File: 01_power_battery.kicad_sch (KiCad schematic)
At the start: 144 parts, among them Q13 CSD19537Q3 100V AUX reverse F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, Q14 BSS138 fast reverse-gate pull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, Q21 SiSS4409DN 40V reverse-blocki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, Q22 SiSS4409DN 40V reverse-blocki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, Q23 SiSS4409DN 40V reverse-blocki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, Q24 SiSS4409DN 40V reverse-blocki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, Q25 CSD17575Q3 BQ25798 ship FET, Q26 SiSS4409DN 40V reverse-blocki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, Q27 SiSS4409DN 40V reverse-blocki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, Q28 SiSS4409DN 40V reverse-blocki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, Q29 SiSS4409DN 40V reverse-blocki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, Q700 BSS138 source and cell-temper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, Q702 BSS138 QON open-drain pulse, U10 BQ34Z100-G1 protected-pack ga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, U12 TPS26630RGER 3A AUX eFuse / s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, U15 LTC4418IUF#PBF dual-input sel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, U16 LTC4418IUF#PBF dual-input sel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, U2 BQ25798RQMR, U2210 SN74LVC1G08DBVR charger reque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, U718 TPS26600RHFR aggregate AON eF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

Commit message: rework the board placement and fix more power stuff
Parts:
- removed D710, D712, D713: B340A 3A 40V EC always-on OR, Diode_SMD:D_SMA, symbol Device:D_Schottky
- removed D715: BAT54WS case button to charger QON, Diode_SMD:D_SOD-323, symbol Device:D_Schottky
- removed R17: 47.0k 0.02% 5ppm ILIM top (3.0A nominal setting), Resistor_SMD:R_0603_1608Metric, symbol Device:R
- removed R190: 100k 0.02% 5ppm ILIM bottom, Resistor_SMD:R_0603_1608Metric, symbol Device:R
- removed R705: 7.50k 1% fixed-valid TS bottom, Resistor_SMD:R_0603_1608Metric, symbol Device:R
- added C2600: 4.7u 50V X7R DCIN, Capacitor_SMD:C_1206_3216Metric, symbol Device:C
- added C2601: 4.7u 10V X7R VDDP, Capacitor_SMD:C_0805_2012Metric, symbol Device:C
- added C2602: 1n 50V C0G PROG filter, Capacitor_SMD:C_0402_1005Metric, symbol Device:C
- added C2603: 100n 50V input sense filter, Capacitor_SMD:C_0402_1005Metric, symbol Device:C
- added C2604: 100n 50V battery sense filter, Capacitor_SMD:C_0402_1005Metric, symbol Device:C
- added C2605: 22n 50V C0G forward compensation, Capacitor_SMD:C_0805_2012Metric, symbol Device:C
- added C2606: 47n 50V X7R reverse compensation, Capacitor_SMD:C_0603_1608Metric, symbol Device:C
- added C2607: 220n 50V X7R current monitor, Capacitor_SMD:C_0603_1608Metric, symbol Device:C
- added C2608, C2609: 100u 35V hybrid system bulk, Capacitor_SMD:CP_Elec_6.3x7.7, symbol Device:C_Polarized
- added C2620, C2621, C2650: 100n 50V charge pump, Capacitor_SMD:C_0603_1608Metric, symbol Device:C
- added C2622: 22n 50V C0G retry timer, Capacitor_SMD:C_0805_2012Metric, symbol Device:C
- added C2641, C2642, C2643: 100n 50V bypass, Capacitor_SMD:C_0603_1608Metric, symbol Device:C
- added C2651: 1u 50V protected input bypass, Capacitor_SMD:C_0603_1608Metric, symbol Device:C
- added C2660: 22n 50V C0G gate ramp, Capacitor_SMD:C_0805_2012Metric, symbol Device:C
- added C2661, C2662: 1u 50V fault timer, Capacitor_SMD:C_0603_1608Metric, symbol Device:C
- added C2685: 100n 50V U15 V2 local, Capacitor_SMD:C_0603_1608Metric, symbol Device:C
- added D2600, D2601: BAT54WS bias OR, Diode_SMD:D_SOD-323, symbol Device:D_Schottky
- added D2620: BAT54WS fast gate discharge, Diode_SMD:D_SOD-323, symbol Device:D_Schottky
- added D2640: BAT54S AUX ADC rail clamps, Package_TO_SOT_SMD:SOT-23, symbol BMS_Thermal:BAT54S_AKC
- added Q2600, Q2601, Q2602, Q2603: CSD17577Q3A 30V switching FET, ducktop2:CSD17577Q3A_DNH, symbol Q_NMOS_123S_4G_5678D:Q_NMOS_123S_4G_5678D
- added Q2604, Q2605: BSS138, Package_TO_SOT_SMD:SOT-23, symbol Q_NMOS_SOT23_GSD:Q_NMOS_SOT23_GSD
- added Q2620, Q2621, Q2622, Q2623, Q2650: CSD19537Q3 100V, ducktop2:CSD19537Q3_DQG, symbol Q_NMOS_123S_4G_5678D:Q_NMOS_123S_4G_5678D
- added Q2644: BSS138 AUX discharge, Package_TO_SOT_SMD:SOT-23, symbol Q_NMOS_SOT23_GSD:Q_NMOS_SOT23_GSD
- added Q2660: CSD18540Q5B AON pass FET, ducktop2:CSD18540Q5B_DNK, symbol Q_NMOS_123S_4G_5678D:Q_NMOS_123S_4G_5678D
- added R2600: 100k BGATE to source, Resistor_SMD:R_0603_1608Metric, symbol Device:R
- added R2601: 10R DCIN filter, Resistor_SMD:R_0603_1608Metric, symbol Device:R
- added R2602: 4.7R VDDP filter, Resistor_SMD:R_0603_1608Metric, symbol Device:R
- added R2603, R2604, R2605, R2606: 0R gate link, Resistor_SMD:R_0603_1608Metric, symbol Device:R
- added R2607: 2R input sense filter, Resistor_SMD:R_0402_1005Metric, symbol Device:R
- added R2608: 1k forward compensation, Resistor_SMD:R_0402_1005Metric, symbol Device:R
- added R2609: 1k reverse compensation, Resistor_SMD:R_0402_1005Metric, symbol Device:R
- added R2610: 4.53k current monitor filter, Resistor_SMD:R_0402_1005Metric, symbol Device:R
- added R2611: 20k PSYS monitor load, Resistor_SMD:R_0402_1005Metric, symbol Device:R
- added R2612: 100k throttle default-on, Resistor_SMD:R_0603_1608Metric, symbol Device:R
- added R2620: 10k gate ramp resistor, Resistor_SMD:R_0603_1608Metric, symbol Device:R
- added R2640: 100k 1% bias sense top, Resistor_SMD:R_0603_1608Metric, symbol Device:R
- added R2641: 24.9k 1% bias sense bottom, Resistor_SMD:R_0603_1608Metric, symbol Device:R
- added R2642: 10k bias-good pull-up, Resistor_SMD:R_0603_1608Metric, symbol Device:R
- added R2643: 100k PROCHOT sense default-low, Resistor_SMD:R_0603_1608Metric, symbol Device:R
- added R2644: 10k AUX permission series, Resistor_SMD:R_0603_1608Metric, symbol Device:R
- added R2645: 47k AUX permission default-off, Resistor_SMD:R_0603_1608Metric, symbol Device:R
- added R2646: 1k 1W switched AUX discharge, Resistor_SMD:R_2512_6332Metric, symbol Device:R
- added R2647: 100k discharge gate default-low, Resistor_SMD:R_0603_1608Metric, symbol Device:R
- added R2661: 10R gate damping, Resistor_SMD:R_0402_1005Metric, symbol Device:R
- added R2662, RS2660: 180m 1% 0.25W parallel AON shunt, Resistor_SMD:R_1206_3216Metric, symbol Device:R
- added R2663: 100k always-on enable, Resistor_SMD:R_0603_1608Metric, symbol Device:R
- added R2664: 1k gate-ramp branch, Resistor_SMD:R_0603_1608Metric, symbol Device:R
- added RS2600: 20m 1% 2W input Kelvin shunt, Resistor_SMD:R_2512_6332Metric, symbol Device:R
- added RS2601: 10m 1% 2W battery Kelvin shunt, Resistor_SMD:R_2512_6332Metric, symbol Device:R
- added RS2620: 22m 1% 2W AON Kelvin shunt, Resistor_SMD:R_2512_6332Metric, symbol Device:R
- added TP2660: AON reset, TestPoint:TestPoint_Pad_D1.5mm, symbol Connector:TestPoint
- added TP2661: GND, TestPoint:TestPoint_Pad_D1.5mm, symbol Connector:TestPoint
- added U2620, U2621: LM74700QDBVRQ1, Package_TO_SOT_SMD:SOT-23-6, symbol Power_Management:LM74700
- added U2634: TPS3700DDCR charger-bias detector, Package_TO_SOT_SMD:SOT-23-6, symbol TPS3700:TPS3700
- added U2635: TCA9537DGSR power status and AUX control, Package_SO:MSOP-10_3x3mm_P0.5mm, symbol Interface_Expansion:PCA9537
- added U2644: SN74LVC1G04DBVR AUX discharge, Package_TO_SOT_SMD:SOT-23-5, symbol 74xGxx:74LVC1G04
- added U2650: LM74700QDBVRQ1 system standby feed, Package_TO_SOT_SMD:SOT-23-6, symbol Power_Management:LM74700
- added U2660: LTC4231IMS-1#PBF standby current limiter, Package_SO:MSOP-12_3x4.039mm_P0.65mm, symbol LTC4231-1:LTC4231-1
- C10: value 100n 50V X7R PMID local -> 1u 50V input local; MPN GRM188R71H104KA93D -> GRT188R61H105ME13D
- C11: value 100n 50V X7R SYS local -> 1u 50V system local; MPN GRM188R71H104KA93D -> GRT188R61H105ME13D
- C2260: value 100n 50V charger-temperature AND bypass -> 100n 50V AND bypass
- C7: value 47n 25V X7R BTST1 -> 470n 25V X7R bootstrap; footprint Capacitor_SMD:C_0402_1005Metric -> Capacitor_SMD:C_0603_1608Metric; MPN GRM155R71E473KA88D -> C1608X7R1E474K080AE; Manufacturer Murata -> TDK
- C701, C702: value 10u 25V X7R VBUS -> 10u 50V X7R input; MPN GRM31CR71E106KA12L -> CGA5L1X7R1H106K160AC; Manufacturer Murata -> TDK
- C703, C704, C705: value 10u 25V X7R PMID -> 10u 50V X7R input; MPN GRM31CR71E106KA12L -> CGA5L1X7R1H106K160AC; Manufacturer Murata -> TDK
- C706, C707, C708, C709, C710: value 10u 25V X7R SYS -> 10u 25V X7R system
- C711: value 100n 50V X7R BAT local -> 100n 50V battery voltage filter; footprint Capacitor_SMD:C_0603_1608Metric -> Capacitor_SMD:C_0402_1005Metric; MPN GRM188R71H104KA93D -> GRM155R71H104ME14D
- C712, C713: value 10u 25V X7R BAT -> 10u 25V X7R battery
- C714: value 2.2u 25V X7R VBUS hot-plug damper -> 2.2u 50V X7R input damper; MPN GRM21BR71E225KA73L -> MSASU21GBB7225KTNA01; Manufacturer Murata -> Taiyo Yuden
- C715: value 15n 50V stage2 TMR approx 240ms -> 1n 50V C0G stage2 validation; MPN GRM155R71H153KA12D -> GRM1555C1H102JA01D
- C740: value 100n 10V INTVCC -> 100n 50V INTVCC; MPN GRM188R71A104KA61D -> GRM188R71H104KA93D
- C741: value 15n 50V TMR approx 240ms -> 1n 50V C0G selector validation; MPN GRM155R71H153KA12D -> GRM1555C1H102JA01D
- C749: value 100n 10V stage2 INTVCC -> 100n 50V stage2 INTVCC; MPN GRM188R71A104KA61D -> GRM188R71H104KA93D
- C795: value 1u 25V AON eFuse input -> 1u 50V AON input; footprint Capacitor_SMD:C_0805_2012Metric -> Capacitor_SMD:C_0603_1608Metric; MPN GRM21BR71H105KA12L -> GRT188R61H105ME13D
- C796: value 100n 50V AON eFuse input local -> 100n 50V AON input local
- C797: value 10u 25V AON eFuse output -> 100u 35V hybrid AON hold-up; footprint Capacitor_SMD:C_1206_3216Metric -> Capacitor_SMD:CP_Elec_6.3x7.7; symbol Device:C -> Device:C_Polarized; MPN GRM31CR71E106KA12L -> EEHZK1V101XP; Manufacturer Murata -> Panasonic
- C798: value 100n 50V AON eFuse output local -> 100n 50V AON output local
- C799: value 22n 50V C0G 5% AON eFuse dVdt -> 22n 50V C0G gate ramp
- C8: value 47n 25V X7R BTST2 -> 470n 25V X7R bootstrap; footprint Capacitor_SMD:C_0402_1005Metric -> Capacitor_SMD:C_0603_1608Metric; MPN GRM155R71E473KA88D -> C1608X7R1E474K080AE; Manufacturer Murata -> TDK
- C9: value 4.7u 10V X7R REGN -> 4.7u 10V X7R VDD
- D711: value B340A 3A 40V EC always-on OR -> SS310 3A 100V AUX standby feed; MPN B340A-13-F -> SS310-13-F
- D716: value BAT54WS case button to Mu PWRBTN -> BAT54WS case button to Mu
- L1: value 1.0uH 20% 28A Isat BQ25798 1.5MHz -> 2.2uH 20%; 31A Isat30; footprint Inductor_SMD:L_Coilcraft_XAL7030-102 -> ducktop2:Coilcraft_XGL1060_Center; MPN XAL7030-102MEC -> XGL1060-222MEC
- LED1: value Charge STAT -> Adapter absent
- Q25: value CSD17575Q3 BQ25798 ship FET -> CSD17575Q3 battery power-path FET
- Q700: value BSS138 source and cell-temperature qualified charger enable -> BSS138
- Q702: value BSS138 QON open-drain pulse -> BSS138
- R12: value 1k -> 2.2k adapter-status LED; MPN RC0603FR-071KL -> RC0603FR-072K2L
- R13: value 100k QON-control gate pulldown -> 100k throttle-release default-low
- R14: value 10k CE hardware-disable pull-up to REGN -> 100k NTC-inhibit default-on; MPN RC0603FR-0710KL -> RC0603FR-07100KL
- R15: value 10k INT pull-up to 3V3 -> 10k charger interrupt pull-up
- R16: value 5.24k 1% fixed-valid TS top -> 10k fixed-valid NTC resistance; MPN RC0603FR-075K24L -> RC0603FR-0710KL
- R18: value 10.5k 1% PROG: 3S, 1.5MHz -> 2.21k 0.1% 25ppm 3S / 724kHz / 200mA startup; footprint Resistor_SMD:R_0603_1608Metric -> Resistor_SMD:R_0402_1005Metric; MPN RC0603FR-0710K5L -> TNPW04022K21BEED; Manufacturer Yageo -> Vishay
- R2260: value 1k isolated temperature-permit input series -> 1k temperature-permit input
- R2261: value 100k temperature-permit input default-low -> 100k temperature-permit default-low
- R2262: value 4.7k charger-enable output fail-off pulldown -> 4.7k charge-permit default-low
- R2263: value 100k pack-fault input defaults to fault when control cable is absent -> 100k pack-fault default-low
- R30: value 4.7k I2C SCL pull-up to 3V3 -> 4.7k SCL pull-up
- R31: value 4.7k I2C SDA pull-up to 3V3 -> 4.7k SDA pull-up
- R704: value 100R BATP Kelvin filter -> 100R battery voltage filter; footprint Resistor_SMD:R_0603_1608Metric -> Resistor_SMD:R_0402_1005Metric; MPN RC0603FR-07100RL -> RC0402FR-07100RL
- R706: value 2R VBUS hot-plug damper -> 2.2R input damper; MPN RC0603FR-072RL -> RC0603FR-072R2L
- R719: value 100k charger-enable gate pulldown -> 100k charge request default-low
- R730: value 1.00M 0.1% USB UV top -> 75.0k 0.02% 5ppm UV top; MPN RT0603BRD071ML -> TNPU060375K0HZEN00; Manufacturer Yageo -> Vishay
- R731: value 35.7k 0.02% 5ppm USB window middle -> 23.2k 0.02% 5ppm window middle; MPN TNPU060335K7HZEN00 -> TNPU060323K2HZEN00
- R732: value 47.5k 0.02% 5ppm USB OV bottom -> 4.53k 0.02% 5ppm OV bottom; MPN TNPU060347K5HZEN00 -> TNPU06034K53HZEN00
- R741: value 1.00M 0.1% PD2 UV top -> 75.0k 0.02% 5ppm UV top; MPN RT0603BRD071ML -> TNPU060375K0HZEN00; Manufacturer Yageo -> Vishay
- R742: value 35.7k 0.02% 5ppm PD2 window middle -> 23.2k 0.02% 5ppm window middle; MPN TNPU060335K7HZEN00 -> TNPU060323K2HZEN00
- R743: value 47.5k 0.02% 5ppm PD2 OV bottom -> 4.53k 0.02% 5ppm OV bottom; MPN TNPU060347K5HZEN00 -> TNPU06034K53HZEN00
- R744: value 383k 0.1% stage2 UV top -> 75.0k 0.02% 5ppm UV top; MPN RT0603BRD07383KL -> TNPU060375K0HZEN00; Manufacturer Yageo -> Vishay
- R745: value 54.9k 0.02% 5ppm stage2 window middle -> 23.2k 0.02% 5ppm window middle; MPN TNPU060354K9HZEN00 -> TNPU060323K2HZEN00
- R746: value 20.0k 0.02% 5ppm stage2 OV bottom -> 4.53k 0.02% 5ppm OV bottom; MPN TNPU060320K0HZEN00 -> TNPU06034K53HZEN00
- R795: value 8.06k 0.02% 5ppm AON UV/OV top -> 56.2k 0.02% 5ppm AON UV top; MPN TNPU06038K06HZEN00 -> TNPU060356K2HZEN00
- R796: value 1.43k 0.02% 5ppm AON UV/OV middle -> 8.25k 0.02% 5ppm AON UV bottom; MPN TNPU06031K43HZEN00 -> TNPU06038K25HZEN00
- R797: value 511R 0.02% 5ppm AON UV/OV bottom -> 100k 0.02% 5ppm AON OV top; MPN TNPU0603511RHZEN00 -> TNPU0603100KHZEN00
- R798: value 16k 0.02% 5ppm; parallel pair gives 8k AON ILIM -> 2.15k 0.02% 5ppm AON OV bottom; MPN TNPU060316K0HZEN00 -> TNPU06032K15HZEN00
- R799: value 16k 0.02% 5ppm; parallel pair gives 8k AON ILIM -> 100k standby enable pull-up; MPN TNPU060316K0HZEN00 -> RC0603FR-07100KL; Manufacturer Vishay -> Yageo
- RS1: MPN WSLP2512R0050FEA -> WSLP25125L000FEA
- U2: value BQ25798RQMR -> ISL9241IRTZ; footprint Package_DFN_QFN:Texas_RQM0029A_VQFN-29_4x4mm_P0.4mm -> ducktop2:Renesas_L32_4x4D_QFN32_EP2.7; symbol ducktop2:BQ25798 -> ISL9241:ISL9241; MPN BQ25798RQMR -> ISL9241IRTZ; Manufacturer Texas Instruments -> Renesas
- U2210: value SN74LVC1G08DBVR charger request AND isolated cell-temperature permit -> SN74LVC1G08DBVR
- U718: value TPS26600RHFR aggregate AON eFuse with 20V recovery margin -> LTC4368IMS-2#PBF standby breaker; footprint Package_DFN_QFN:Texas_RHF0024A_VQFN-24-1EP_4x5mm_P0.5mm_EP2.65x3.65mm -> Package_SO:MSOP-10_3x3mm_P0.5mm; symbol Power_Management:TPS26600RHF -> LTC4368-2:LTC4368-2; MPN TPS26600RHFR -> LTC4368IMS-2#PBF; Manufacturer Texas Instruments -> Analog Devices
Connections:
- net AON_EFUSE_OV: now also R797.2, R798.1, U718.3 (OV); no longer R796.2, R797.1, U718.12 (OVP)
- net AON_EFUSE_UV: now also U718.2 (UV); no longer U718.10 (UVLO)
- net AON_FAULT_N: now also U718.7 (FAULT), U2660.9 (STATUS); no longer U718.22 (~{FLT})
- net AUX_DC_ADC: now also D2640.3 (K1_A2)
- net AUX_DC_FUSED: now also D711.2 (A), R191.1
- net AUX_DC_PROTECTED: now also R2646.1; no longer D711.2 (A)
- net AUX_EFUSE_IN_SYS: no longer R191.1
- net BATP_SENSE: now also C711.1, U2.31 (VBAT); no longer U2.18 (BATP)
- net BTST1_NODE: now also U2.12 (BOOT1); no longer U2.4 (BTST1)
- net BTST2_NODE: now also U2.4 (BOOT2); no longer U2.19 (BTST2)
- net CHG_ENABLE_THERM: now also Q702.1 (G); no longer Q700.1 (G)
- net CHG_INT_N: now also U2.26 (CMOUT/~{INT}); no longer U2.21 (~{INT})
- net EC_AON_IN: now also Q2660.1 (S), Q2660.2 (S), Q2660.3 (S), U2660.11 (SOURCE); no longer U718.23 (OUT), U718.24 (OUT)
- net GND: now also R16.2, R796.2, R798.2, U2.20 (OTGEN/CMIN), U2.33 (GND), U718.5 (GND), C2600.2, C2601.2, C2602.2, C2605.2, C2606.2, C2607.2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; no longer U2.10 (ACDRV2), U2.11 (ACDRV1), U2.27 (GND), U718.17 (GND)
- net I2C_SCL: now also U2.22 (SCL), U2635.8 (SCL); no longer U2.14 (SCL)
- net I2C_SDA: now also U2.21 (SDA), U2635.9 (SDA); no longer U2.15 (SDA)
- net MCU_3V3: now also C2641.1, C2642.1, C2643.1, D2640.2 (K2), R2642.1, U2634.5 (VDD), U2635.10 (VDD), U2644.5 (VCC)
- net PACK_CHG_TEMP_OK_IN: now also U2635.3 (IO2)
- net PACK_POS_FUSED: now also C712.1, C713.1, Q25.1 (S), Q25.2 (S), Q25.3 (S), R2600.2; no longer Q25.5 (D(5-8))
- net PD1_VBUS_RAW: now also C2620.2, Q2620.1 (S), Q2620.2 (S), Q2620.3 (S), U2620.3 (EN), U2620.6 (ANODE)
- net PD2_VBUS_RAW: now also C2621.2, Q2621.1 (S), Q2621.2 (S), Q2621.3 (S), U2621.3 (EN), U2621.6 (ANODE)
- net PROG_SET: now also U2.19 (PROG), C2602.1; no longer U2.20 (PROG)
- net REGN: now also U2.18 (VDD), R2602.1, R2612.1, R2640.1; no longer R16.1, U2.5 (REGN)
- net SEL_STAGE2: now also C2685.1
- net SW1: now also U2.10 (PHASE1), Q2600.1 (S), Q2600.2 (S), Q2600.3 (S), Q2601.5 (D(5-8)); no longer U2.28 (SW1)
- net SW2: now also U2.6 (PHASE2), Q2602.5 (D(5-8)), Q2603.1 (S), Q2603.2 (S), Q2603.3 (S); no longer U2.26 (SW2)
- net VBUS_COMBINED: now also R2607.1, RS2600.1; no longer C701.1, C702.1, U2.2 (VBUS), U2.3 (VBUS), U2.8 (VAC2), U2.9 (VAC1)
- net VSYS: now also U2.2 (CSOP), C2604.1, C2608.1, C2609.1, C2650.2, D2601.2 (A), Q2603.5 (D(5-8)), Q2650.1 (S), Q2650.2 (S), Q2650.3 (S), RS2601.1, U2650.3 (EN)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; no longer U2.25 (SYS)
- net AON_RAW: now reaches U718.1 (VIN)
- net AON_RAW: now also C795.1, C796.1, D711.1 (K), R795.1, R797.1, R799.1, Q2620.5 (D(5-8)), Q2621.5 (D(5-8)), Q2622.5 (D(5-8)), Q2650.5 (D(5-8)), U2620.4 (CATHODE), U2621.4 (CATHODE)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
- net AON_RETRY: now reaches U718.4 (RETRY)
- net AON_RETRY: now also C2622.1
- net AON_PROTECT_SHDN: now reaches U718.6 (SHDN)
- net AON_PROTECT_SHDN: now also R799.2
- net AUX_EFUSE_SHDN: now reaches U12.12 (~{SHDN})
- net AUX_EFUSE_SHDN: now also R2644.2, R2645.1
- net CHG_LS2_DRV: now reaches U2.7 (LGATE2)
- net CHG_LS2_DRV: now also R2605.1
- net AON_EFUSE_DVDT renamed AON_FET_GATE
- net AON_FET_GATE: now also D2620.2 (A), Q2622.4 (G), Q2623.4 (G), R2620.2; no longer U718.20 (dVdT)
- removed net AON_EFUSE_ILM: R798.1, R799.1, U718.19 (ILIM)
- removed net AON_EFUSE_RTN: C799.2, R797.2, R798.2, R799.2, U718.13 (MODE), U718.15 (RTN), U718.25 (RTN)
- removed net AON_OR_RAW: C795.1, C796.1, D711.1 (K), R795.1, U718.8 (IN), U718.9 (IN)
- removed net BAT_CHARGER: C711.1, C712.1, C713.1, Q25.1 (S), Q25.2 (S), Q25.3 (S), U2.22 (BAT), U2.23 (BAT)
- removed net CHG_CE_HW_N: Q700.3 (D), R14.2, U2.13 (~{CE})
- net CHG_TS_FIXED: no longer names the net of U2.16 (BYPSG)
- net CHG_TS_FIXED: no longer R16.2
- net ILIM_SET renamed CHG_DCIN
- net CHG_DCIN: now also C2600.1, R2601.2
- net PMIC_QON_ASSERT renamed MU_PROCHOT_RELEASE
- net MU_PROCHOT_RELEASE: now also Q2605.1 (G); no longer Q702.1 (G)
- net PMIC_QON_PIN renamed CHG_NTC_HOT_GATE
- net CHG_NTC_HOT_GATE: now also Q700.1 (G), R14.2; no longer U2.12 (~{QON})
- net PMID renamed CHG_INPUT
- net CHG_INPUT: now also C701.1, C702.1, U2.14 (CSIN), C2603.2, D2600.2 (A), Q2600.5 (D(5-8)), RS2600.2; no longer U2.29 (PMID)
- net SDRV_GATE renamed CHG_ACOK
- net CHG_ACOK: now also LED1.1 (K); no longer Q25.4 (G)
- net STAT_DRV renamed CHG_SRN
- net CHG_SRN: now also Q25.5 (D(5-8)), C2604.2, RS2601.2; no longer LED1.1 (K)
- new net AON_FET_COMMON: Q2622.1 (S), Q2622.2 (S), Q2622.3 (S), Q2623.1 (S), Q2623.2 (S), Q2623.3 (S)
- new net AON_GATE_DRV: D2620.1 (K), R2620.1, U718.10 (GATE)
- new net AON_LIMIT_DRV: R2661.1, R2664.1, U2660.12 (GATE)
- new net AON_LIMIT_GATE: Q2660.4 (G), R2661.2
- new net AON_LIMIT_RAMP: C2660.1, R2664.2
- new net AON_LIMIT_SENSE: Q2660.5 (D(5-8)), R2662.2, RS2660.2, U2660.1 (SENSE)
- new net AON_LIMIT_SHDN: R2663.2, TP2660.1, U2660.3 (SHDN)
- new net AON_LIMIT_TIMER: C2661.1, C2662.1, U2660.10 (TIMER)
- new net AON_PD1_GATE: Q2620.4 (G), U2620.5 (GATE)
- new net AON_PD1_VCAP: C2620.1, U2620.1 (VCAP)
- new net AON_PD2_GATE: Q2621.4 (G), U2621.5 (GATE)
- new net AON_PD2_VCAP: C2621.1, U2621.1 (VCAP)
- new net AON_PROTECTED: C2651.1, C799.2, R2662.1, R2663.1, RS2620.2, RS2660.1, U2660.2 (IN), U2660.4 (UVL), U2660.5 (UVH), U718.8 (VOUT)
- new net AON_PROTECT_SENSE: Q2623.5 (D(5-8)), RS2620.1, U718.9 (SENSE)
- new net AON_SYS_GATE: Q2650.4 (G), U2650.5 (GATE)
- new net AON_SYS_VCAP: C2650.1, U2650.1 (VCAP)
- new net AUX_DISCHARGE: Q2644.1 (G), R2647.1, U2644.4
- new net AUX_DISCHARGE_DRAIN: Q2644.3 (D), R2646.2
- new net AUX_PATH_EN: R2644.1, U2635.1 (IO0), U2644.2
- new net CHG_BGATE: Q25.4 (G), R2600.1, U2.32 (BGATE)
- new net CHG_BIAS_GOOD: R2642.2, U2634.1 (OUTA), U2635.2 (IO1)
- new net CHG_BIAS_OR: D2600.1 (K), D2601.1 (K), R2601.1
- new net CHG_BIAS_SENSE: R2640.2, R2641.1, U2634.3 (INA+)
- new net CHG_COMPF: R2608.1, U2.28 (COMPF)
- new net CHG_COMPF_RC: C2605.1, R2608.2
- new net CHG_COMPR: R2609.1, U2.27 (COMPR)
- new net CHG_COMPR_RC: C2606.1, R2609.2
- new net CHG_CSIP: C2603.1, R2607.2, U2.15 (CSIP)
- new net CHG_HS1_DRV: R2603.1, U2.11 (UGATE1)
- new net CHG_HS1_GATE: Q2600.4 (G), R2603.2
- new net CHG_HS2_DRV: R2606.1, U2.5 (UGATE2)
- new net CHG_HS2_GATE: Q2603.4 (G), R2606.2
- new net CHG_IMON: R2610.1, U2.29 (AMON/BMON)
- new net CHG_IMON_FILTER: C2607.1, R2610.2
- new net CHG_LS1_DRV: R2604.1, U2.9 (LGATE1)
- new net CHG_LS1_GATE: Q2601.4 (G), R2604.2
- new net CHG_LS2_GATE: Q2602.4 (G), R2605.2
- new net CHG_NTC: Q700.3 (D), R16.1, U2.25 (BATGONE/NTC)
- new net CHG_PSYS: R2611.1, U2.30 (PSYS)
- new net CHG_THROTTLE_GATE: Q2604.1 (G), Q2605.3 (D), R2612.2
- new net CHG_VDDP: C2601.1, R2602.2, U2.13 (BYPSRC), U2.8 (VDDP)
- new net MU_PROCHOT_N: Q2604.3 (D), R2643.1, U2.23 (~{PROCHOT}), U2635.4 (IO3)
- new net NRST_NET: U2635.6 (~{RESET})
- no-connect marks 27 -> 18
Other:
- note added: "5V and 9V adapters use the buck-boost path. Running and charging share the measured input budget; a qualified pack can cover a shortfall."
- note added: "== U2 ISL9241: 3S NVDC charger and system supply =="
- note added: "== U2660 standby current limit and service reset =="
- note added: "== always-on supply: low-loss USB feeds and shared protection =="
- note added: "== source-control interlocks =="
- note added: "A low bias indication means REGN is below about 2V, beneath the charger reset threshold. Wait for detector startup before using it."
- note added: "A powered charger must acknowledge a low input limit before any source is enabled. An I2C failure alone is not proof of reset."
- note added: "After fixing a standby short, remove all power or momentarily short TP2660 to TP2661 to reset the latch. This also restarts the EC."
- note added: "BMS J2: 1 raw negative, 2 cell2 tap, 3 raw positive, 4 cell1 tap. Verify the assembled harness before connecting cells."
- note added: "Charge current and VSYSMIN power up at zero. Check JEITA, 3S strap, current limits and throttle before releasing the hardware gates."
- note added: "ISL9241 starts with a 200mA input limit and charging off. Firmware must verify the source and program bounded limits."
- note added: "Q25 is the NVDC battery FET. Shutdown disables the loads; this FET alone does not provide complete pack isolation."
- note added: "RS2600 is the 20mOhm input shunt. RS2601 is the separate 10mOhm battery-current shunt; both need Kelvin routing."
- note added: "Raw USB/AUX can start the EC before source selection. VSYS supplies standby from the adapter or protected pack."
- note added: "STARTUP: keep Mu enable low and PROCHOT asserted. Read TCPC PD Status 0x40 and active PDO/RDO 0x34/0x35 before selecting a source."
- note added: "The combined sense resistance is 90mOhm. Kelvin-route IN and SENSE to the resistor pair; no load copper in the pickups."
- note added: "U15/U16 accepts fixed 5/9/15/20V PD contracts and AUX across 7-22V; priority remains PD1 > PD2 > AUX."
- note added: "U718 provides fast voltage protection. U2660 controls inrush and latches a sustained overcurrent. Both start without the EC."
- note added: "U718 supplies the fast UV/OV protection. U2660 UV/OV inputs are disabled; its current limiter and timer remain active."
- note added: "USB and VSYS use reverse-blocking ideal-diode feeds. AUX uses D711. The EC can start from 5V USB before the main source paths are enabled."
- note removed: "A 5V-only USB-C source leaves the laptop off. AON_FAULT_N inhibits charging and Mu start; the service connector remains the assembly hard disconnect."
- note removed: "AON UV rising remains above 6.0 V, so default 5 V USB-C is negotiation-only. B340A input OR blocks DC negative sources; transient overshoot still needs measurement."
- note removed: "AUX_DC_ADC measures the post-reverse-FET input so firmware can detect droop and reduce BQ25798 input current."
- note removed: "BQ25798 /CE requires CHG_ENABLE AND isolated PACK_CHG_TEMP_OK. REGN pulls /CE high when either permit is absent."
- note removed: "BQ25798 TS remains fixed at 58.9% REGN with TS_IGNORE=0. BQ34Z100 uses TEMPS=0; its internal temperature is not a cell-temperature measurement."
- note removed: "BQ25798 keeps TS_IGNORE=0 and STOP_WD_CHG=1. TS divider is not a cell sensor; raw BMS CTRs and isolated /CE gating provide cell-temperature inhibits."
- note removed: "J190 is the one 7-22V nominal AUX/solar input; TPS26630 protects it before BQ25798."
- note removed: "J2: pins 1/2 PACK+, pins 3/4 PACK-, pin 5 cell1 tap, pin 6 cell2 tap. Verify harness order before first connection."
- note removed: "Q25 follows BQ25798EVM-842: SDRV disconnects pack discharge for electronic ship/hard-off while adapter charging can wake the pack."
- note removed: "SMCJ24CA protects the 67V eFuse input; active OVP protects the BQ25798 24V recommended input limit."
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
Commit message: finish the new bms and move the connectors up top
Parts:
- removed C2260: 100n 50V AND bypass, Capacitor_SMD:C_0603_1608Metric, symbol Device:C
- removed F190: 3A MINI AUX input fuse: Littelfuse 0297003.WXNV, Fuse:Fuseholder_Blade_Mini_Keystone_3568, symbol Device:Fuse
- removed L1: 2.2uH 20%; 31A Isat30, ducktop2:Coilcraft_XGL1060_Center, symbol Device:L
- removed Q23: SiSS4409DN 40V reverse-blocking PMOS, Package_SO:Vishay_PowerPAK_1212-8_Single, symbol Q_PMOS_1G_234S_5D:Q_PMOS_1G_234S_5D
- removed Q2602: CSD17577Q3A 30V switching FET, ducktop2:CSD17577Q3A_DNH, symbol Q_NMOS_123S_4G_5678D:Q_NMOS_123S_4G_5678D
- removed R16: 10k fixed-valid NTC resistance, Resistor_SMD:R_0603_1608Metric, symbol Device:R
- removed R2260: 1k temperature-permit input, Resistor_SMD:R_0603_1608Metric, symbol Device:R
- removed R2261: 100k temperature-permit default-low, Resistor_SMD:R_0603_1608Metric, symbol Device:R
- removed R719: 100k charge request default-low, Resistor_SMD:R_0603_1608Metric, symbol Device:R
- removed R734: 63.4k 0.02% 5ppm AUX window middle, Resistor_SMD:R_0603_1608Metric, symbol Device:R
- removed R742: 23.2k 0.02% 5ppm window middle, Resistor_SMD:R_0603_1608Metric, symbol Device:R
- removed U15: LTC4418IUF#PBF dual-input selector (stage 1), ducktop2:ADI_UF20_QFN20_4x4_P0.5_EP2.45, symbol LTC4418IUF:LTC4418IUF
- removed U2210: SN74LVC1G08DBVR, Package_TO_SOT_SMD:SOT-23-5, symbol 74xGxx:74LVC1G08
- added C798: 100n 50V AON output local, Capacitor_SMD:C_0603_1608Metric, symbol Device:C
- added Q14: BSS138 fast reverse-gate pulldown, Package_TO_SOT_SMD:SOT-23, symbol Q_NMOS_SOT23_GSD:Q_NMOS_SOT23_GSD
- added Q29: SiSS4409DN 40V reverse-blocking PMOS, Package_SO:Vishay_PowerPAK_1212-8_Single, symbol Q_PMOS_1G_234S_5D:Q_PMOS_1G_234S_5D
- added Q700, Q702: BSS138, Package_TO_SOT_SMD:SOT-23, symbol Q_NMOS_SOT23_GSD:Q_NMOS_SOT23_GSD
- added R718: 10k main AUX VALID pull-up, Resistor_SMD:R_0603_1608Metric, symbol Device:R
- added TP1: GND test, TestPoint:TestPoint_Pad_D1.0mm, symbol Connector:TestPoint
- added TP9: CHG_INT_N test, TestPoint:TestPoint_Pad_D1.0mm, symbol Connector:TestPoint
- F190: renamed from Q29; value SiSS4409DN 40V reverse-blocking PMOS -> 3A MINI AUX input fuse: Littelfuse 0297003.WXNV; footprint Package_SO:Vishay_PowerPAK_1212-8_Single -> Fuse:Fuseholder_Blade_Mini_Keystone_3568; symbol Q_PMOS_1G_234S_5D:Q_PMOS_1G_234S_5D -> Device:Fuse; MPN SiSS4409DN-T1-GE3 -> 0297003.WXNV + 3568; Manufacturer Vishay -> Littelfuse / Keystone
- L1: renamed from Q700; value BSS138 -> 2.2uH 20%; 31A Isat30; footprint Package_TO_SOT_SMD:SOT-23 -> ducktop2:Coilcraft_XGL1060_Center; symbol Q_NMOS_SOT23_GSD:Q_NMOS_SOT23_GSD -> Device:L; MPN BSS138LT1G -> XGL1060-222MEC; Manufacturer onsemi -> Coilcraft
- Q23: renamed from C798; value 100n 50V AON output local -> SiSS4409DN 40V reverse-blocking PMOS; footprint Capacitor_SMD:C_0603_1608Metric -> Package_SO:Vishay_PowerPAK_1212-8_Single; symbol Device:C -> Q_PMOS_1G_234S_5D:Q_PMOS_1G_234S_5D; MPN GRM188R71H104KA93D -> SiSS4409DN-T1-GE3; Manufacturer Murata -> Vishay
- Q2602: renamed from Q702; value BSS138 -> CSD17577Q3A 30V switching FET; footprint Package_TO_SOT_SMD:SOT-23 -> ducktop2:CSD17577Q3A_DNH; symbol Q_NMOS_SOT23_GSD:Q_NMOS_SOT23_GSD -> Q_NMOS_123S_4G_5678D:Q_NMOS_123S_4G_5678D; MPN BSS138LT1G -> CSD17577Q3A; Manufacturer onsemi -> Texas Instruments
- R16: renamed from Q14; value BSS138 fast reverse-gate pulldown -> 10k fixed-valid NTC resistance; footprint Package_TO_SOT_SMD:SOT-23 -> Resistor_SMD:R_0603_1608Metric; symbol Q_NMOS_SOT23_GSD:Q_NMOS_SOT23_GSD -> Device:R; MPN BSS138LT1G -> RC0603FR-0710KL; Manufacturer onsemi -> Yageo
- R2262: value 4.7k charge-permit default-low -> 4.7k charge request default-low
- R2263: value 100k pack-fault default-low -> 100k monitor-ready default-low
- R734: renamed from TP9; value CHG_INT_N test -> 63.4k 0.02% 5ppm AUX window middle; footprint TestPoint:TestPoint_Pad_D1.0mm -> Resistor_SMD:R_0603_1608Metric; symbol Connector:TestPoint -> Device:R; MPN (none) -> TNPU060363K4HZEN00; Manufacturer (none) -> Vishay; ProcurementClass PCB copper test feature -> (none); now in the parts list
- R742: renamed from TP1; value GND test -> 23.2k 0.02% 5ppm window middle; footprint TestPoint:TestPoint_Pad_D1.0mm -> Resistor_SMD:R_0603_1608Metric; symbol Connector:TestPoint -> Device:R; MPN (none) -> TNPU060323K2HZEN00; Manufacturer (none) -> Vishay; ProcurementClass PCB copper test feature -> (none); now in the parts list
- TP10: value PACK_FAULT_N test -> PACK_MONITOR_READY test
- U15: renamed from R718; value 10k main AUX VALID pull-up -> LTC4418IUF#PBF dual-input selector (stage 1); footprint Resistor_SMD:R_0603_1608Metric -> ducktop2:ADI_UF20_QFN20_4x4_P0.5_EP2.45; symbol Device:R -> LTC4418IUF:LTC4418IUF; MPN RC0603FR-0710KL -> LTC4418IUF#PBF; Manufacturer Yageo -> Analog Devices
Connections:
- net AUX_DC_FUSED: now also F190.2
- net AUX_DC_PROTECTED: now also Q23.5 (D(5-8))
- net AUX_DC_RAW: now also F190.1
- net AUX_EFUSE_BGATE: now also Q14.3 (D); no longer R16.3 (D)
- net AUX_EFUSE_IN_SYS: now also Q14.2 (S); no longer R16.2 (S)
- net AUX_EFUSE_Q2_GATE: now also Q14.1 (G); no longer R16.1 (G)
- net CHG_ENABLE: now also R2262.1, Q702.1 (G)
- net CHG_INT_N: now also TP9.1; no longer R734.1
- net CHG_LS2_GATE: now also Q2602.4 (G)
- net CHG_NTC: now also R16.1, Q700.3 (D); no longer L1.3 (D)
- net CHG_NTC_HOT_GATE: now also Q700.1 (G), Q702.3 (D); no longer L1.1 (G), Q2602.3 (D)
- net EC_AON_IN: now also C798.1; no longer Q23.1
- net GND: now also Q2602.1 (S), Q2602.3 (S), R16.2, U15.20 (HYS), U15.21 (EP/GND), U15.8 (GND), C798.2, Q700.2 (S), Q702.2 (S), TP1.1; no longer L1.2 (S), Q23.2, R742.1
- net MAIN_AUX_VALID_N: now also U15.7 (~{VALID2}), R718.2; no longer U15.2
- net MAIN_SEL_INTVCC: now also U15.10 (INTVCC), U15.18 (EN), U15.19 (~{SHDN})
- net MAIN_SEL_TMR: now also U15.1 (TMR)
- net MAIN_USB_VALID_N: now also U15.6 (~{VALID1})
- net MCU_3V3: now also R718.1; no longer U15.1
- net SEL_STAGE2: now also U15.16 (V2)
- net ST2_AUX_FET_COMMON: now also Q23.2 (S), Q23.3 (S), Q23.4 (S)
- net ST2_AUX_GATE: now also Q23.1 (G)
- net ST2_AUX_OV: now also R734.2
- net ST2_AUX_UV: now also R734.1
- net ST2_MAIN_FET_COMMON: now also U15.12 (VS2), Q29.2 (S), Q29.3 (S), Q29.4 (S); no longer F190.2 (S), F190.3 (S), F190.4 (S)
- net ST2_MAIN_GATE: now also U15.11 (G2), Q29.1 (G); no longer F190.1 (G)
- net ST2_MAIN_OV: now also U15.5 (OV2)
- net ST2_MAIN_UV: now also U15.4 (UV2)
- net ST2_USB_OV: now also R742.2
- net ST2_USB_UV: now also R742.1
- net SW1: now also L1.1
- net SW2: now also L1.2, Q2602.5 (D(5-8))
- net USB_MAIN_FET_COMMON: now also U15.14 (VS1)
- net USB_MAIN_GATE: now also U15.13 (G1)
- net USB_MAIN_OV: now also U15.3 (OV1)
- net USB_MAIN_UV: now also U15.2 (UV1)
- net USB_PD_SELECTED: now also U15.17 (V1)
- net VBUS_COMBINED: now also U15.15 (VOUT), Q29.5 (D(5-8)); no longer F190.5 (D(5-8))
- removed net CHG_ENABLE_THERM: Q2602.1 (G), R2262.1
- net PACK_CHG_TEMP_OK_IN: no longer names the net of U2635.3 (IO2)
- net PACK_FAULT_N renamed PACK_MONITOR_READY
- no-connect marks 18 -> 19
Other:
- note added: "AUX current is limited by the released source profile. Solar MPPT is not implemented in this charger driver."
- note added: "AUX_DC_ADC measures the protected input so firmware can detect droop and reduce charger input current."
- note added: "BMS J2 carries raw pack power; J2201 carries the two midpoint taps. Verify connector polarity before connecting cells."
- note added: "Charging requires verified BMS status and bounded EC source/current settings. The raw BMS charge inhibit remains independent."
- note added: "FPC-3 to BMS: protected pack power and isolated I2C/alarm cross here"
- note added: "J190 is the one 7-22V nominal AUX input; TPS26630 protects it before the source selector."
- note added: "Q25 is the ISL9241 battery-path FET. Battery standby comes through VSYS and the discharge shunt; disabling Mu keeps button wake available."
- note added: "RS11 is a four-terminal2mOhm shunt. Independent current guards, native cell/current protection and F1 cover the battery path."
- note added: "SMCJ24CA protects the AUX eFuse input. The common LTC4418 window protects the charger input."
- note added: "The charger NTC pin receives a hardware inhibit from the BMS permit. The fixed 10k state is not a cell-temperature measurement."
- note added: "The charger watchdog stays enabled. JEITA, source limits and throttle settings must be read back before the hardware gates are released."
- note added: "Three insulated cell probes drive independent raw-referenced charge/discharge inhibits on the BMS."
- note added: "U718 provides fast voltage protection. U2660 limits standby inrush and latches a persistent fault; TP2660/TP2661 provide a service reset."
- note added: "U719 BQ76922 protects the three cells and drives high-side charge/discharge FETs from its verified configuration."
- note removed: "== U2 bq25798 Buck-Boost Charger / NVDC Power Path (VSYS) =="
- note removed: "BMS J2: 1 raw negative, 2 cell2 tap, 3 raw positive, 4 cell1 tap. Verify the assembled harness before connecting cells."
- note removed: "FPC-3 to BMS: PACK_POS_FUSED / PACK_FAULT_N / PACK_RETRY_PULSE cross here"
- note removed: "RS11=8mOhm gives 7.5A nominal OCD and 15A nominal SCD; U11/RS10 and F1 remain independent tighter/secondary protection."
- note removed: "Three insulated cell probes drive raw-referenced BMS comparators and CTRC/CTRD. U719 TS retains its unused-function strap."
- note removed: "U719 BQ7791500 autonomously protects each cell at 4.20V OV / 2.90V UV and drives back-to-back low-side FETs."
- moved on the sheet: L1

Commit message: finish the keyboard and update the case and power
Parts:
- C2606: MPN GRM188R71H473KA61D -> C0603C473K5RACTU; Manufacturer Murata -> KEMET
- C720: MPN GRM21BR71H105KA01 -> C2012X7R1H105K125AB; Manufacturer Murata -> TDK
- R2600: value 100k BGATE to source -> 1M BGATE to source; MPN RC0603FR-07100KL -> RC0603FR-071ML
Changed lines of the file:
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@@
   (dnp no)
   (property "Reference" "R2600" (at 1089.66 237.49 0) (effects (font (size 1.27 1.27))))
-  (property "Value" "100k BGATE to source" (at 1089.66 242.57 0) (effects (font (size 1.27 1.27))))
+  (property "Value" "1M BGATE to source" (at 1089.66 242.57 0) (effects (font (size 1.27 1.27))))
   (property "Footprint" "Resistor_SMD:R_0603_1608Metric" (at 1089.66 240.03 0) (effects (font (size 1.27 1.27)) (hide yes)))
   (property "Datasheet" "" (at 1089.66 240.03 0) (effects (font (size 1.27 1.27)) (hide yes)))
   (property "Manufacturer" "Yageo" (at 1089.66 240.03 0) (effects (font (size 1.27 1.27)) (hide yes)))
-  (property "MPN" "RC0603FR-07100KL" (at 1089.66 240.03 0) (effects (font (size 1.27 1.27)) (hide yes)))
+  (property "MPN" "RC0603FR-071ML" (at 1089.66 240.03 0) (effects (font (size 1.27 1.27)) (hide yes)))
   (pin "1")
   (pin "2")
@@
   (property "Footprint" "Capacitor_SMD:C_0603_1608Metric" (at 1089.66 384.81 0) (effects (font (size 1.27 1.27)) (hide yes)))
   (property "Datasheet" "" (at 1089.66 384.81 0) (effects (font (size 1.27 1.27)) (hide yes)))
-  (property "Manufacturer" "Murata" (at 1089.66 384.81 0) (effects (font (size 1.27 1.27)) (hide yes)))
-  (property "MPN" "GRM188R71H473KA61D" (at 1089.66 384.81 0) (effects (font (size 1.27 1.27)) (hide yes)))
+  (property "Manufacturer" "KEMET" (at 1089.66 384.81 0) (effects (font (size 1.27 1.27)) (hide yes)))
+  (property "MPN" "C0603C473K5RACTU" (at 1089.66 384.81 0) (effects (font (size 1.27 1.27)) (hide yes)))
   (pin "1")
   (pin "2")
@@
   (property "Footprint" "Capacitor_SMD:C_0805_2012Metric" (at 379.73 190.5 0) (effects (font (size 1.27 1.27)) (hide yes)))
   (property "Datasheet" "" (at 379.73 190.5 0) (effects (font (size 1.27 1.27)) (hide yes)))
-  (property "Manufacturer" "Murata" (at 379.73 190.5 0) (effects (font (size 1.27 1.27)) (hide yes)))
-  (property "MPN" "GRM21BR71H105KA01" (at 379.73 190.5 0) (effects (font (size 1.27 1.27)) (hide yes)))
+  (property "Manufacturer" "TDK" (at 379.73 190.5 0) (effects (font (size 1.27 1.27)) (hide yes)))
+  (property "MPN" "C2012X7R1H105K125AB" (at 379.73 190.5 0) (effects (font (size 1.27 1.27)) (hide yes)))
   (pin "1")
   (pin "2")

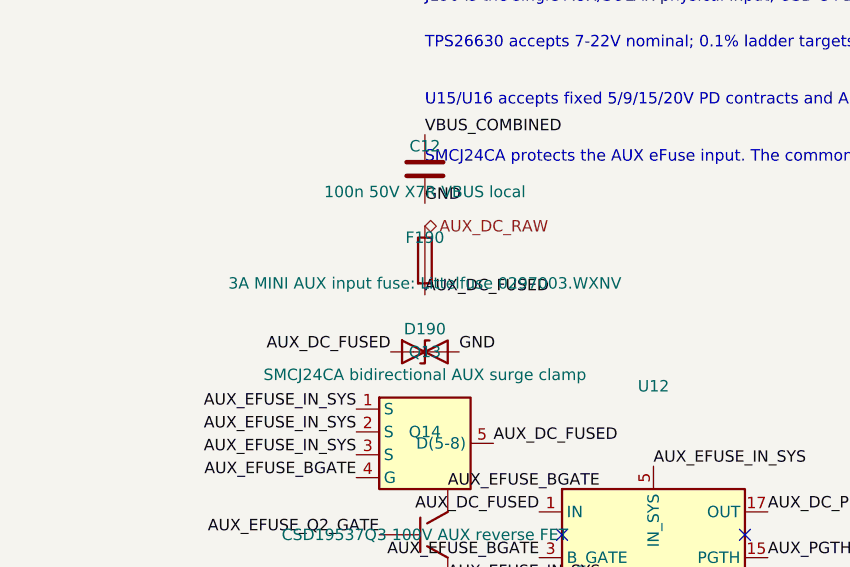
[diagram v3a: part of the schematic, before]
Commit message: lower the aux fuses and check input limits
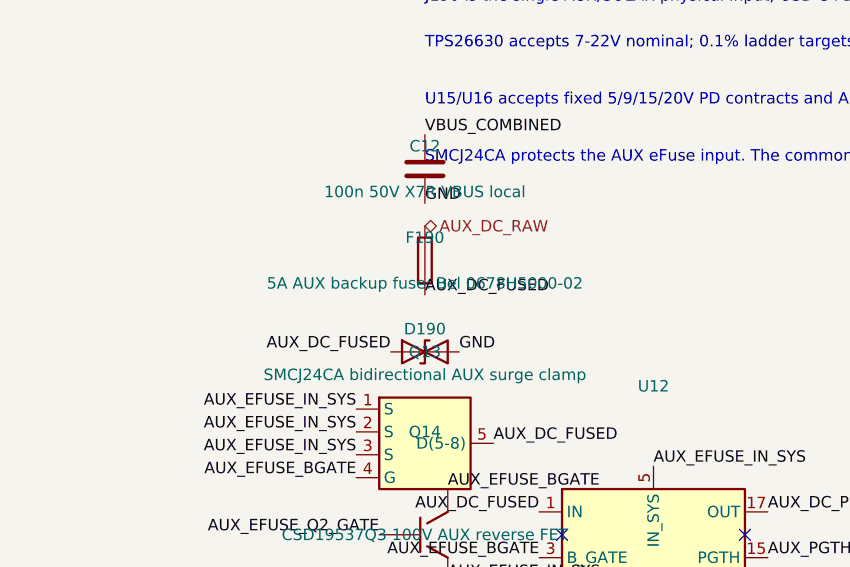
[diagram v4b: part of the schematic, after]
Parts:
- F190: value 3A MINI AUX input fuse: Littelfuse 0297003.WXNV -> 5A AUX backup fuse: Bel 0678H5000-02; footprint Fuse:Fuseholder_Blade_Mini_Keystone_3568 -> ducktop2:Bel_0678H_3912; MPN 0297003.WXNV + 3568 -> 0678H5000-02; Manufacturer Littelfuse / Keystone -> Bel Fuse
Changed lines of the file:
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@@
   (dnp no)
   (property "Reference" "F190" (at 379.73 46.99 0) (effects (font (size 1.27 1.27))))
-  (property "Value" "3A MINI AUX input fuse: Littelfuse 0297003.WXNV" (at 379.73 52.07 0) (effects (font (size 1.27 1.27))))
-  (property "Footprint" "Fuse:Fuseholder_Blade_Mini_Keystone_3568" (at 379.73 49.53 0) (effects (font (size 1.27 1.27)) (hide yes)))
-  (property "Datasheet" "" (at 379.73 49.53 0) (effects (font (size 1.27 1.27)) (hide yes)))
-  (property "Manufacturer" "Littelfuse / Keystone" (at 379.73 49.53 0) (effects (font (size 1.27 1.27)) (hide yes)))
-  (property "MPN" "0297003.WXNV + 3568" (at 379.73 49.53 0) (effects (font (size 1.27 1.27)) (hide yes)))
+  (property "Value" "5A AUX backup fuse: Bel 0678H5000-02" (at 379.73 52.07 0) (effects (font (size 1.27 1.27))))
+  (property "Footprint" "ducktop2:Bel_0678H_3912" (at 379.73 49.53 0) (effects (font (size 1.27 1.27)) (hide yes)))
+  (property "Datasheet" "https://www.belfuse.com/media/datasheets/products/circuit-protection/ds-cp-0678h-series.pdf" (at 379.73 49.53 0) (effects (font (size 1.27 1.27)) (hide yes)))
+  (property "Manufacturer" "Bel Fuse" (at 379.73 49.53 0) (effects (font (size 1.27 1.27)) (hide yes)))
+  (property "MPN" "0678H5000-02" (at 379.73 49.53 0) (effects (font (size 1.27 1.27)) (hide yes)))
   (pin "1")
   (pin "2")
